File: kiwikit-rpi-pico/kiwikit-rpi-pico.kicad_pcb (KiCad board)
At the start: 2 copper layers, 100 x 100 mm, 50 parts, among them J1 Conn_02x04_Odd_Even, J2 Conn_01x03, J3 Conn_01x06, J4 Conn_01x08, J5 Conn_01x09, J6 Conn_01x03, J7 Conn_01x03, SW0 SW_Push, SW1 SW_Push, SW2 SW_Push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

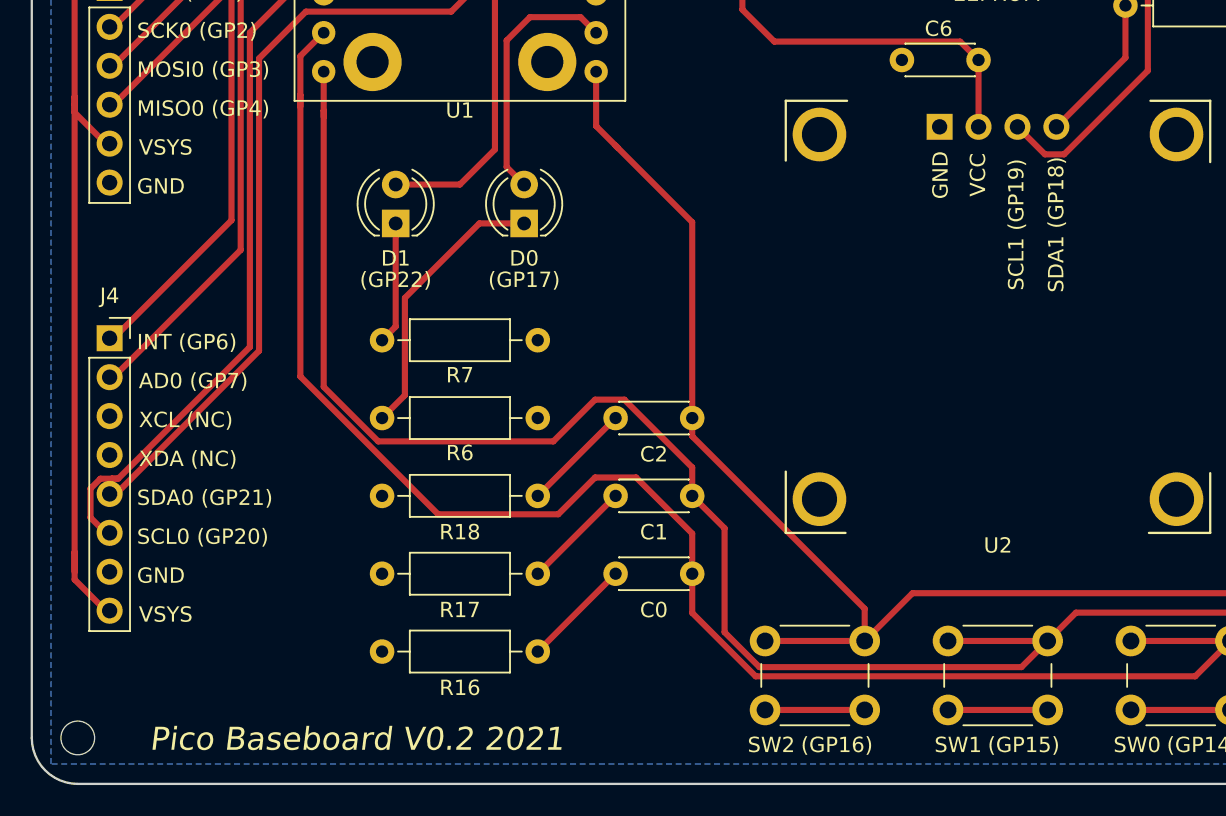
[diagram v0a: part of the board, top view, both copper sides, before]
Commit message: Update to version 0.3, adjust debouncer layout.
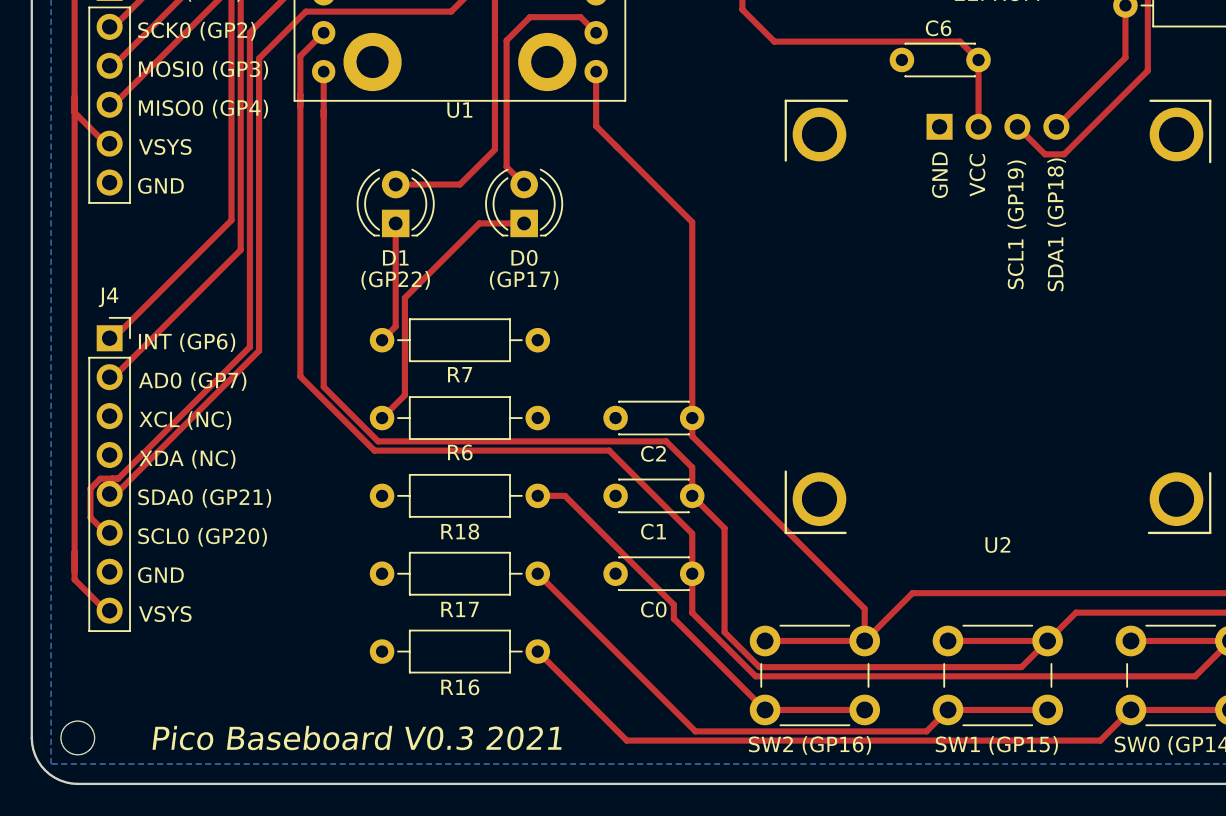
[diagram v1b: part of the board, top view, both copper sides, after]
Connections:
- C0 pad 1: Net-(C0-Pad1) -> GND
- C1 pad 1: Net-(C1-Pad1) -> GND
- C2 pad 1: Net-(C2-Pad1) -> GND
- C5 pad 1: Net-(C5-Pad1) -> GND
- R15 pad 1: Net-(C5-Pad1) -> Net-(R15-Pad1)
- R16 pad 1: Net-(C0-Pad1) -> Net-(R16-Pad1)
- R17 pad 1: Net-(C1-Pad1) -> Net-(R17-Pad1)
- R18 pad 1: Net-(C2-Pad1) -> Net-(R18-Pad1)
- SW0 pad 1: GND -> Net-(R16-Pad1)
- SW1 pad 1: GND -> Net-(R17-Pad1)
- SW2 pad 1: Net-(SW2-Pad1) -> Net-(R18-Pad1)
- SW5 pad 1: GND -> Net-(R15-Pad1)
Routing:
- net Net-(R16-Pad1): track 0.00 -> 48.4 mm
- net Net-(R17-Pad1): track 0.00 -> 38.1 mm
- net Net-(R18-Pad1): track 0.00 -> 27.7 mm
- net GND: track 19.5 -> 0.00 mm
- net Net-(C2-Pad1): track 7.18 -> 0.00 mm
- net Net-(C0-Pad1): track 7.18 -> 0.00 mm
- net Net-(C1-Pad1): track 7.18 -> 0.00 mm
- net Net-(SW2-Pad1): track 6.50 -> 0.00 mm
- net Net-(R15-Pad1): track 0.00 -> 6.50 mm
- net /SW1: track 108.4 -> 106.2 mm
- net /SW0: track 109.7 -> 107.7 mm
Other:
- board text added: "Pico Baseboard V0.3 2021"
- board text removed: "Pico Baseboard V0.2 2021"

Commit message: Generate v0.3 gerbers
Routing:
- net Net-(R15-Pad1): track 6.50 -> 22.4 mm
- net Net-(C5-Pad1): track 7.18 -> 0.00 mm
- net GNDA: track 103.7 -> 100.5 mm
